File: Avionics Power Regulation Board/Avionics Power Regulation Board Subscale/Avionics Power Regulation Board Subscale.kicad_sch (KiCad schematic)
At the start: 15 parts, among them J1 Conn_01x04_Socket, J2 Conn_01x07_Socket, J3 Conn_01x06_Socket, J4 Conn_01x08_Socket, J5 Conn_01x05_Socket, U1 SC0917

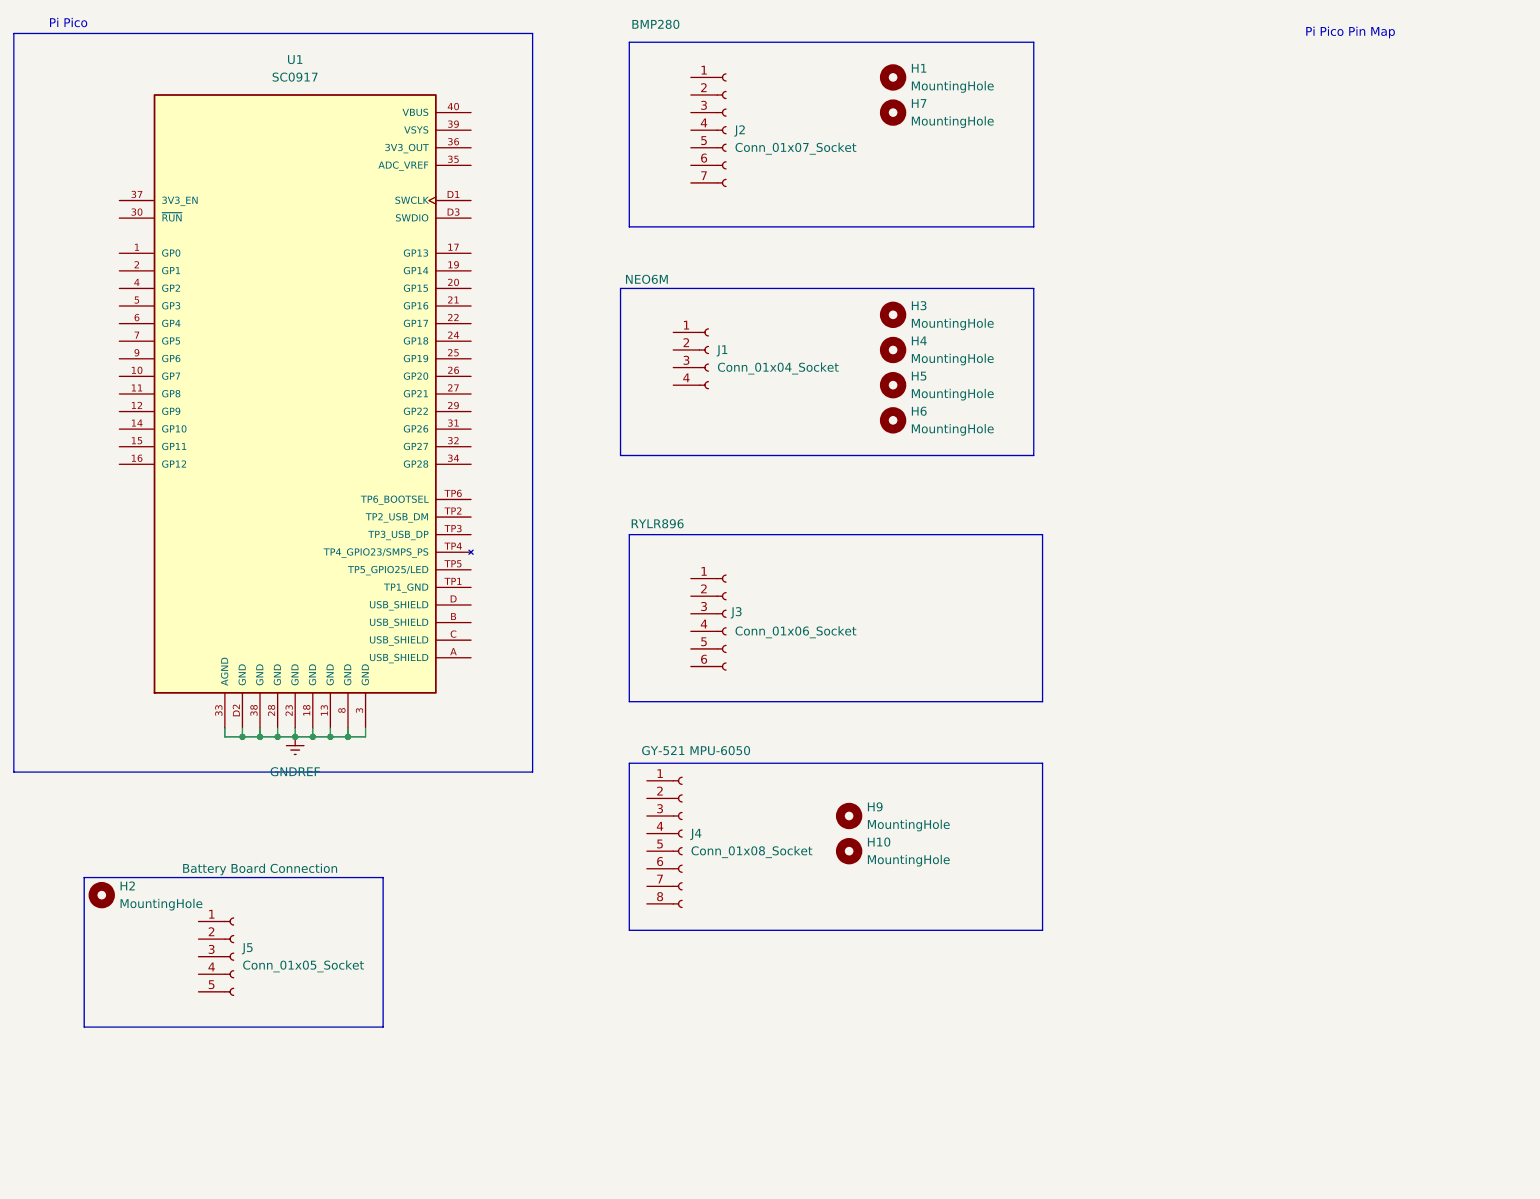
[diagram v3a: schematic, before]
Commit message: Adding to the Avionics Sensors Board
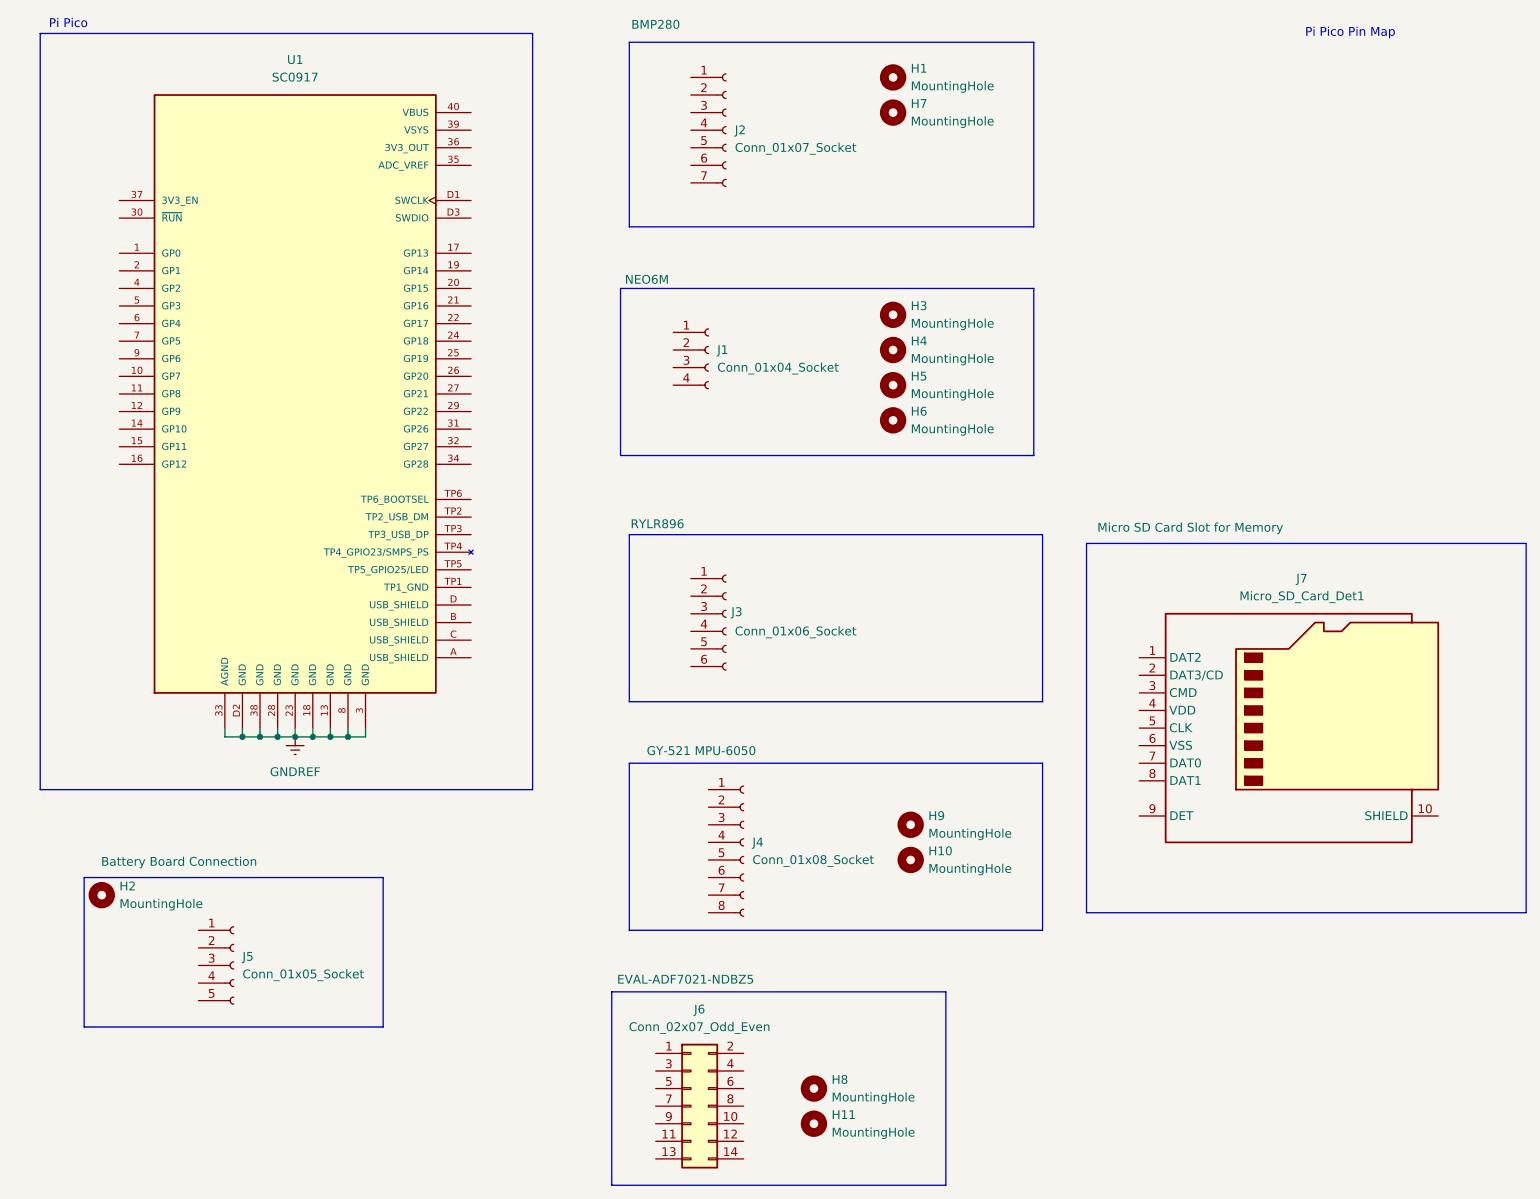
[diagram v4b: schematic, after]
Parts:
- added H11, H8: MountingHole, MountingHole:MountingHole_2.1mm, symbol Mechanical:MountingHole
- added J6: Conn_02x07_Odd_Even, Connector_PinHeader_2.54mm:PinHeader_2x07_P2.54mm_Vertical, symbol Connector_Generic:Conn_02x07_Odd_Even
- added J7: Micro_SD_Card_Det1, symbol Connector:Micro_SD_Card_Det1
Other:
- moved on the sheet: H10, H9, J4, J5
